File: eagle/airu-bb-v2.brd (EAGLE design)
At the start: 86.4 x 54.6 mm, 25 parts, among them U1 BMP180, U2 DHT22, U3 GPS, X2 53261-08

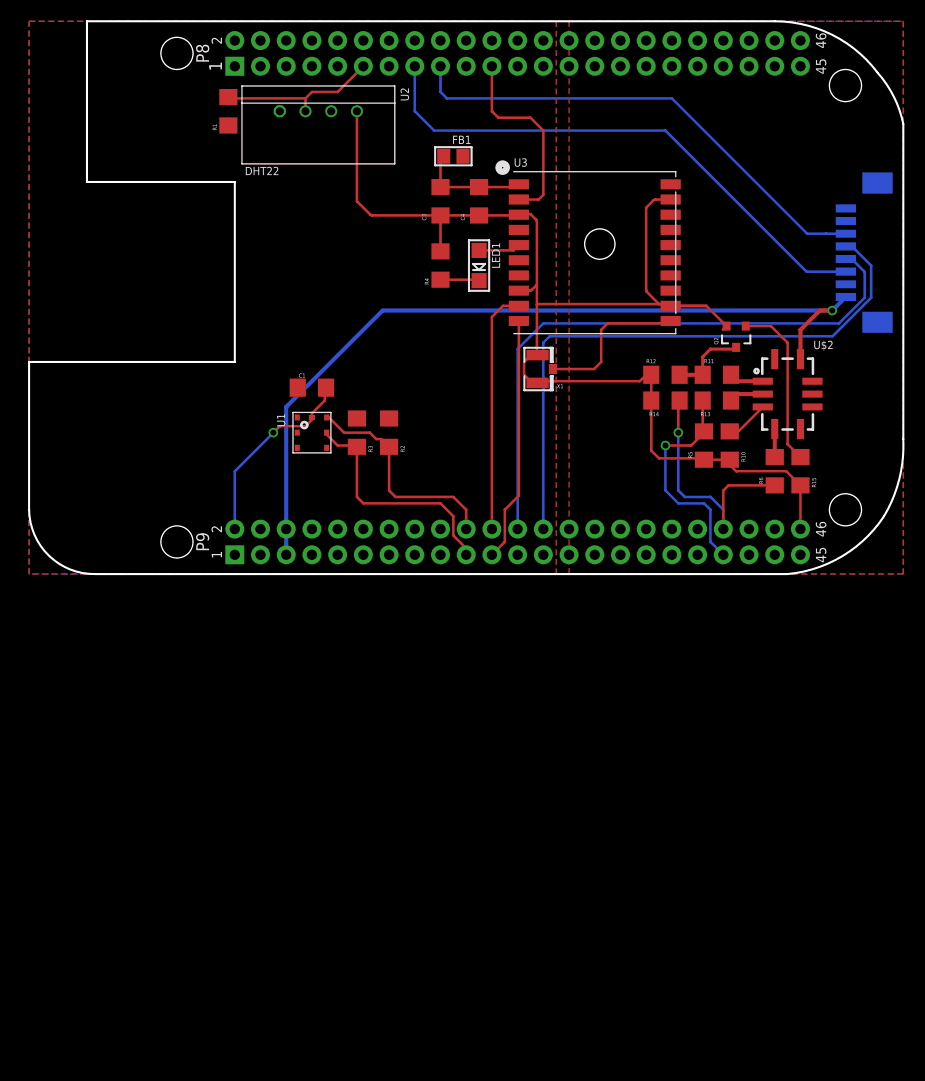
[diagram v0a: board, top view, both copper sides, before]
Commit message: Added SPDT switch for operation mode and added RTC
This commit adds improvements to the schematic which includes a SPDT switch
that will be used to configure the operation mode of the station (lab/field use),
as well as a real-time clock so that time stamps can be used accurately offline.
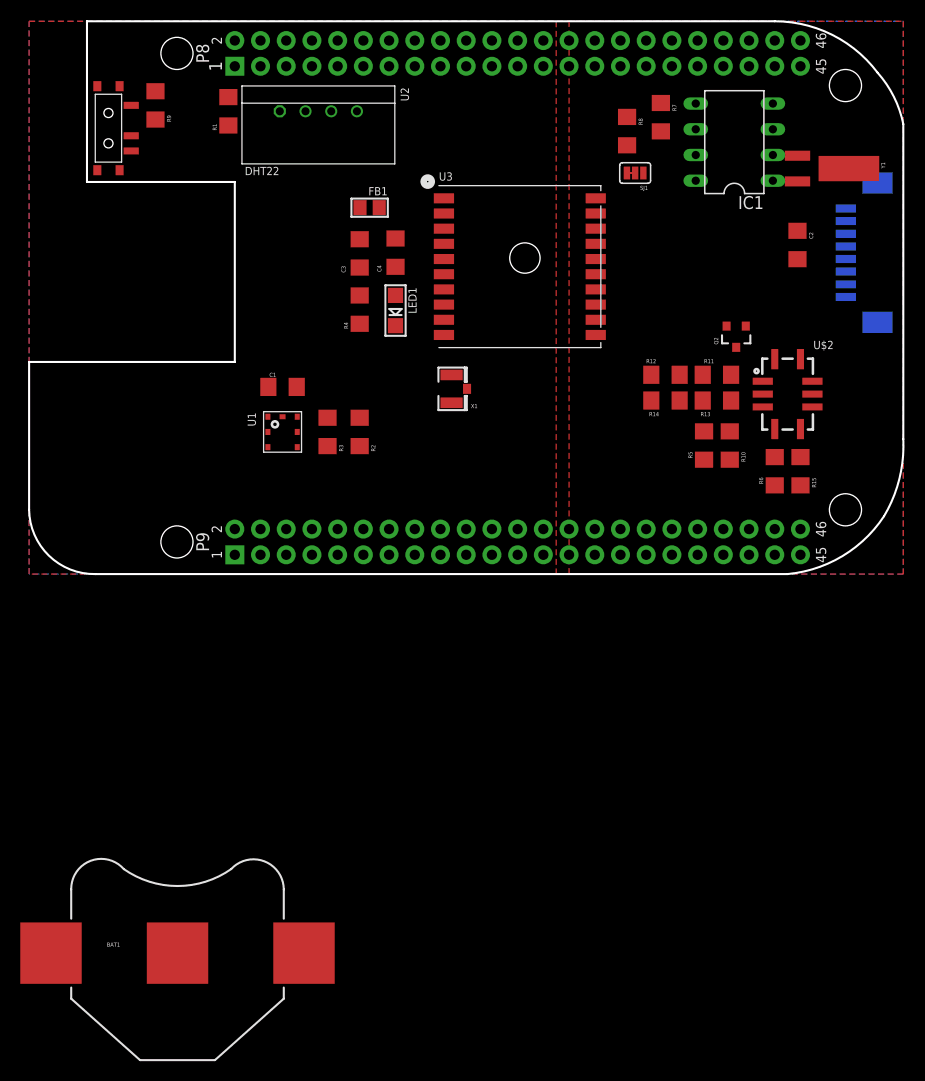
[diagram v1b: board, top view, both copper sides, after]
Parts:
- added BAT1: (no value), SparkFun-Electromechanical:BATTCON_20MM
- added C2: 0.1uF, SparkFun-Passives:1206
- added IC1: DS1307, adafruit:DIL08
- added R7, R8, R9: 10k, SparkFun-Passives:1206
- added SJ1: JUMPER-PAD-3-2OF3_NC_BY_TRACE_SMALL, SparkFun-Passives:PAD-JUMPER-3-2OF3_NC_BY_TRACE_YES_SILK_FULL_BOX
- added U$3: SWITCH_SPDT, SparkFun-Electromechanical:KPS-1290
- added Y1: 32.768kHz, SparkFun-FreqCtrl:CRYSTAL-32KHZ-SMD
- moved FB1 9.71 mm to (33.6, 36.2)
- moved C4 9.69 mm to (36.2, 31.8)
- moved C3 9.50 mm to (32.7, 31.7)
- moved LED1 9.38 mm to (36.2, 26.0)
- moved R4 9.09 mm to (32.7, 26.1)
- moved X1 8.71 mm to (41.7, 18.3)
- moved U3 7.53 mm to (48.5, 30.4)
- moved C1 2.90 mm to (25.0, 18.5)
- moved R2 2.90 mm to (32.7, 14.0)
- moved U1 2.90 mm to (25.0, 14.0)
- moved R3 2.90 mm to (29.5, 14.0)
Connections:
- removed net GPS_NRST: U$1.P8.21, U3.P$2
- removed net PM_RESET: U$1.P8.17, X2.3
- removed net PM_SET: U$1.P8.15, X2.6
- removed net PRE_HEAT_NOX: Q2.1, R15.2
- new net N$11: BAT1.1, IC1.3
- new net N$12: IC1.1, Y1.X2
- new net N$13: R7.2, SJ1.1
- new net N$14: IC1.2, Y1.X1
- new net N$15: R8.2, SJ1.3
- new net OP_MODE: R9.1, U$1.P8.5, U$3.P
- new net PREHEAT_NOX: Q2.1, R15.2, U$1.P8.12
- net 3.3V: now also R9.2
- net 5V: now also C2.2, IC1.8, SJ1.2
- net GND: now also BAT1.2, C2.1, IC1.4, U$3.S
- net SCL: now also IC1.6, R8.1
- net SDA: now also IC1.5, R7.1
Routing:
- net GND: track 143.1 -> 0.00 mm, vias 1 -> 0
- net 5V: track 81.9 -> 0.00 mm, vias 1 -> 0
- net PM_TXD: track 59.1 -> 0.00 mm
- net PM_RXD: track 59.1 -> 0.00 mm
- net PM_SET: track 53.6 -> 0.00 mm
- net PM_RESET: track 48.4 -> 0.00 mm
- net VRED: track 25.3 -> 0.00 mm, vias 1 -> 0
- net GPS_RX: track 24.2 -> 0.00 mm
- net GPS_TX: track 24.1 -> 0.00 mm
- net SCL: track 23.3 -> 0.00 mm
- net VOX: track 22.2 -> 0.00 mm, vias 1 -> 0
- net SDA: track 22.0 -> 0.00 mm
- net GPS_NRST: track 19.3 -> 0.00 mm
- net PRE_HEAT_NOX: track 16.6 -> 0.00 mm
- net DHT_DATA: track 16.0 -> 0.00 mm
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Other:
- board text removed: "02/2016 Jonathan Whitaker"
- board text removed: "V1.0"

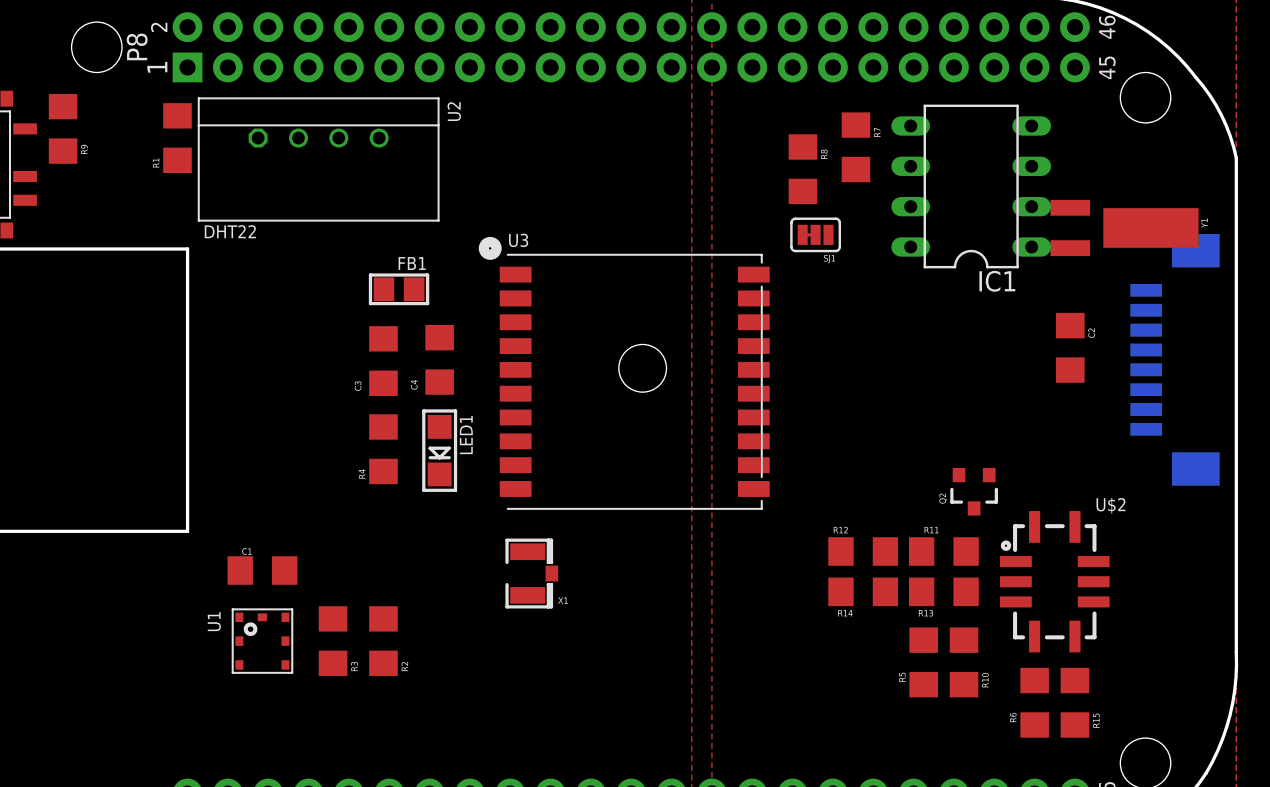
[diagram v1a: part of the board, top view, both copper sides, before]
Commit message: Cleaned up eagle/lib directory.
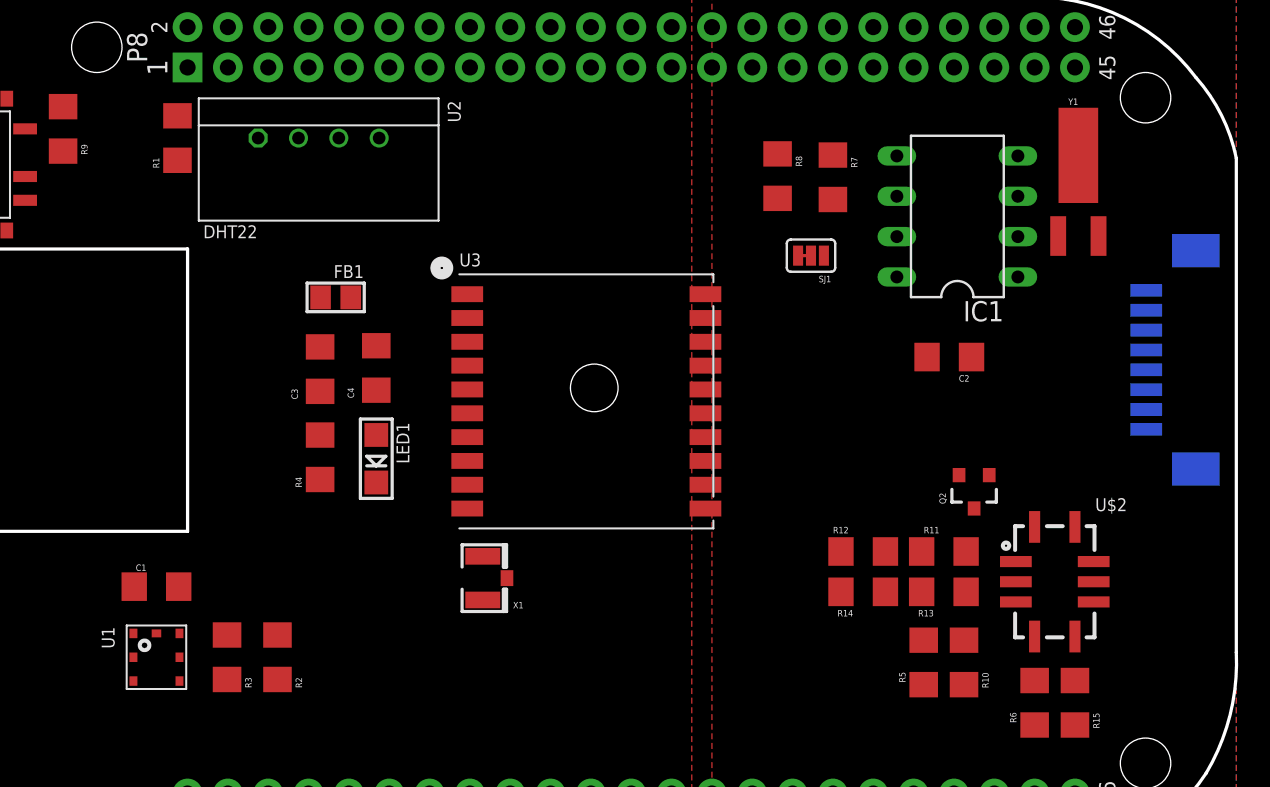
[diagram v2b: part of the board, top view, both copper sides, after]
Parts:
- moved C2 7.64 mm to (68.3, 31.9), turned to 180 degrees
- moved C1 6.75 mm to (18.4, 17.5)
- moved R2 6.75 mm to (26.0, 13.0)
- moved R3 6.75 mm to (22.8, 13.0)
- moved U1 6.75 mm to (18.4, 13.0)
- moved C3 4.02 mm to (28.7, 31.2)
- moved R4 4.02 mm to (28.7, 25.6)
- moved FB1 4.02 mm to (29.6, 35.7)
- moved LED1 4.02 mm to (32.2, 25.5)
- moved C4 4.02 mm to (32.2, 31.2)
- moved U3 3.29 mm to (45.4, 29.1)
- moved X1 2.84 mm to (38.9, 18.0)
- moved R7 2.38 mm to (61.0, 43.3)
- moved IC1 2.08 mm to (68.8, 40.8)
- moved R8 1.65 mm to (57.5, 43.3)
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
